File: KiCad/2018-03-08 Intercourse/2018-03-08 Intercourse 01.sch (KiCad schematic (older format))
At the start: 48 parts

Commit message: minor fixes
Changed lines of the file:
@@
 NoConn ~ 2600 7100
 NoConn ~ 2600 7000
-NoConn ~ 4800 6600
+NoConn ~ 4750 6600
 Text Notes 6300 5300 0    60   Italic 0
 Inter-Card\nConnector
@@
 L VDD #PWR?
 U 1 1 5AB0F171
-P 6100 4800
-F 0 "#PWR?" H 6100 4650 50  0001 C CNN
-F 1 "VDD" H 6100 4950 50  0000 C CNN
-F 2 "" H 6100 4800 50  0001 C CNN
-F 3 "" H 6100 4800 50  0001 C CNN
-	1    6100 4800
+P 6100 4700
+F 0 "#PWR?" H 6100 4550 50  0001 C CNN
+F 1 "VDD" H 6100 4850 50  0000 C CNN
+F 2 "" H 6100 4700 50  0001 C CNN
+F 3 "" H 6100 4700 50  0001 C CNN
+	1    6100 4700
 	1    0    0    -1
 $EndComp
@@
 	4750 6700 5400 6700
 Wire Wire Line
-	4750 6600 4800 6600
-Wire Wire Line
 	3800 5200 3900 5200

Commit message: finailzed schematic with annotations
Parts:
- removed R?: 100K, symbol R_Small
- C?: value 1μF -> 10μF
- R?: value 2K2 -> 17K
- R?: value 3K3 -> 33K
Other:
- note added: "0603\n"
- note added: "0805"
- note added: "0805\n"
- note added: ">15mil"
- note added: "?"
- note added: "X5R/X7R\n0805\n"
- note added: "±1%"
- note added: "±10PPM"
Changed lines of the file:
@@
 U 1 1 5AAA95FB
 P 3100 2100
-F 0 "C?" H 2950 2200 50  0000 L CNN
+F 0 "C?" H 2900 2100 50  0000 L CNN
 F 1 "1μF" H 2900 2000 50  0000 L CNN
 F 2 "" H 3100 2100 50  0001 C CNN
@@
 	1    3100 2100
 	1    0    0    -1
-$EndComp
-$Comp
-L R_Small R?
-U 1 1 5AAAA249
-P 2800 2600
-F 0 "R?" H 2900 2650 50  0000 L CNN
-F 1 "100K" H 2850 2550 50  0000 L CNN
-F 2 "" H 2800 2600 50  0001 C CNN
-F 3 "" H 2800 2600 50  0001 C CNN
-	1    2800 2600
-	-1   0    0    1
 $EndComp
 $Comp
@@
 U 1 1 5AAD1277
 P 4000 5200
-F 0 "Y?" V 3900 5000 50  0000 L CNN
-F 1 "26 MHz" V 4100 4800 50  0000 L CNN
+F 0 "Y?" V 4100 4700 50  0000 L CNN
+F 1 "26 MHz" V 4100 4850 50  0000 L CNN
 F 2 "" H 4000 5200 50  0001 C CNN
 F 3 "" H 4000 5200 50  0001 C CNN
@@
 P 2400 6300
 F 0 "C?" H 2200 6300 50  0000 L CNN
-F 1 "1μF" H 2150 6200 50  0000 L CNN
+F 1 "1μF" H 2200 6200 50  0000 L CNN
 F 2 "" H 2400 6300 50  0001 C CNN
 F 3 "" H 2400 6300 50  0001 C CNN
@@
 $EndComp
 $Comp
-L GND #PWR?
-U 1 1 5AB13EAF
-P 2800 2800
-F 0 "#PWR?" H 2800 2550 50  0001 C CNN
-F 1 "GND" H 2800 2650 50  0000 C CNN
-F 2 "" H 2800 2800 50  0001 C CNN
-F 3 "" H 2800 2800 50  0001 C CNN
-	1    2800 2800
-	1    0    0    -1
-$EndComp
-$Comp
 L VBUS #PWR?
 U 1 1 5AB1587E
@@
 P 5900 5400
 F 0 "C?" V 5950 5450 50  0000 L CNN
-F 1 "1μF" V 6050 5350 50  0000 L CNN
+F 1 "10μF" V 6050 5300 50  0000 L CNN
 F 2 "" H 5900 5400 50  0001 C CNN
 F 3 "" H 5900 5400 50  0001 C CNN
@@
 	3200 2200 3100 2200
 Wire Wire Line
-	2800 2700 2800 2800
-Wire Wire Line
 	4200 2400 4600 2400
 Wire Wire Line
@@
 P 5850 3700
 F 0 "R?" V 5750 3850 50  0000 C CNN
-F 1 "2K2" V 5750 3650 50  0000 C CNN
+F 1 "17K" V 5750 3650 50  0000 C CNN
 F 2 "" V 5780 3700 50  0001 C CNN
 F 3 "" H 5850 3700 50  0001 C CNN
@@
 P 5850 4100
 F 0 "R?" V 5950 4250 50  0000 C CNN
-F 1 "3K3" V 5950 4050 50  0000 C CNN
+F 1 "33K" V 5950 4050 50  0000 C CNN
 F 2 "" V 5780 4100 50  0001 C CNN
 F 3 "" H 5850 4100 50  0001 C CNN
@@
 	6100 3900 6200 3900
 Connection ~ 6200 3900
-Text Notes 6300 4050 0    60   Italic 0
+Text Notes 6300 4000 0    60   Italic 0
 Check if\nconnected\nto USB
 Text GLabel 3100 2600 3    60   Input ~ 0
@@
 Connection ~ 1500 4900
 Wire Wire Line
-	2800 2400 2800 2500
-Connection ~ 2800 2400
-Wire Wire Line
 	3200 2500 3100 2500
 Wire Wire Line
@@
 Wire Wire Line
 	2400 5700 2400 6200
+Text Notes 1200 7050 0    30   ~ 0
+0805
+Text Notes 3900 5450 1    30   ~ 0
+±10PPM
+Text Notes 3600 5100 3    30   ~ 0
+±1%
+Text Notes 1300 6400 0    30   ~ 0
+>15mil
+Text Notes 2300 5500 0    30   ~ 0
+>15mil
+Text Notes 4600 8300 0    30   ~ 0
+>15mil
+Text Notes 2200 6250 0    30   ~ 0
+0805
+Text Notes 1800 6450 0    30   ~ 0
+0603\n
+Text Notes 1600 7050 0    30   ~ 0
+0603\n
+Text Notes 3850 4950 0    30   ~ 0
+0603\n
+Text Notes 4050 4950 0    30   ~ 0
+0603\n
+Text Notes 5900 5150 1    30   ~ 0
+0805\n
+Text Notes 5500 7600 0    30   ~ 0
+0805
+Text Notes 4200 9250 0    30   ~ 0
+0805
+Text Notes 2900 8550 0    30   ~ 0
+0805
+Text Notes 2900 8900 0    30   ~ 0
+0805
+Text Notes 6300 4100 0    30   ~ 0
+0805\n
+Text Notes 4750 2700 2    30   ~ 0
+0805\n
+Text Notes 2900 2050 0    30   ~ 0
+X5R/X7R\n0805\n
+Text Notes 3600 3800 0    30   ~ 0
+0805\n
+Text Notes 5800 5000 0    120  ~ 24
+?
+Text Notes 5400 1500 0    30   ~ 0
+0805\n
 $EndSCHEMATC

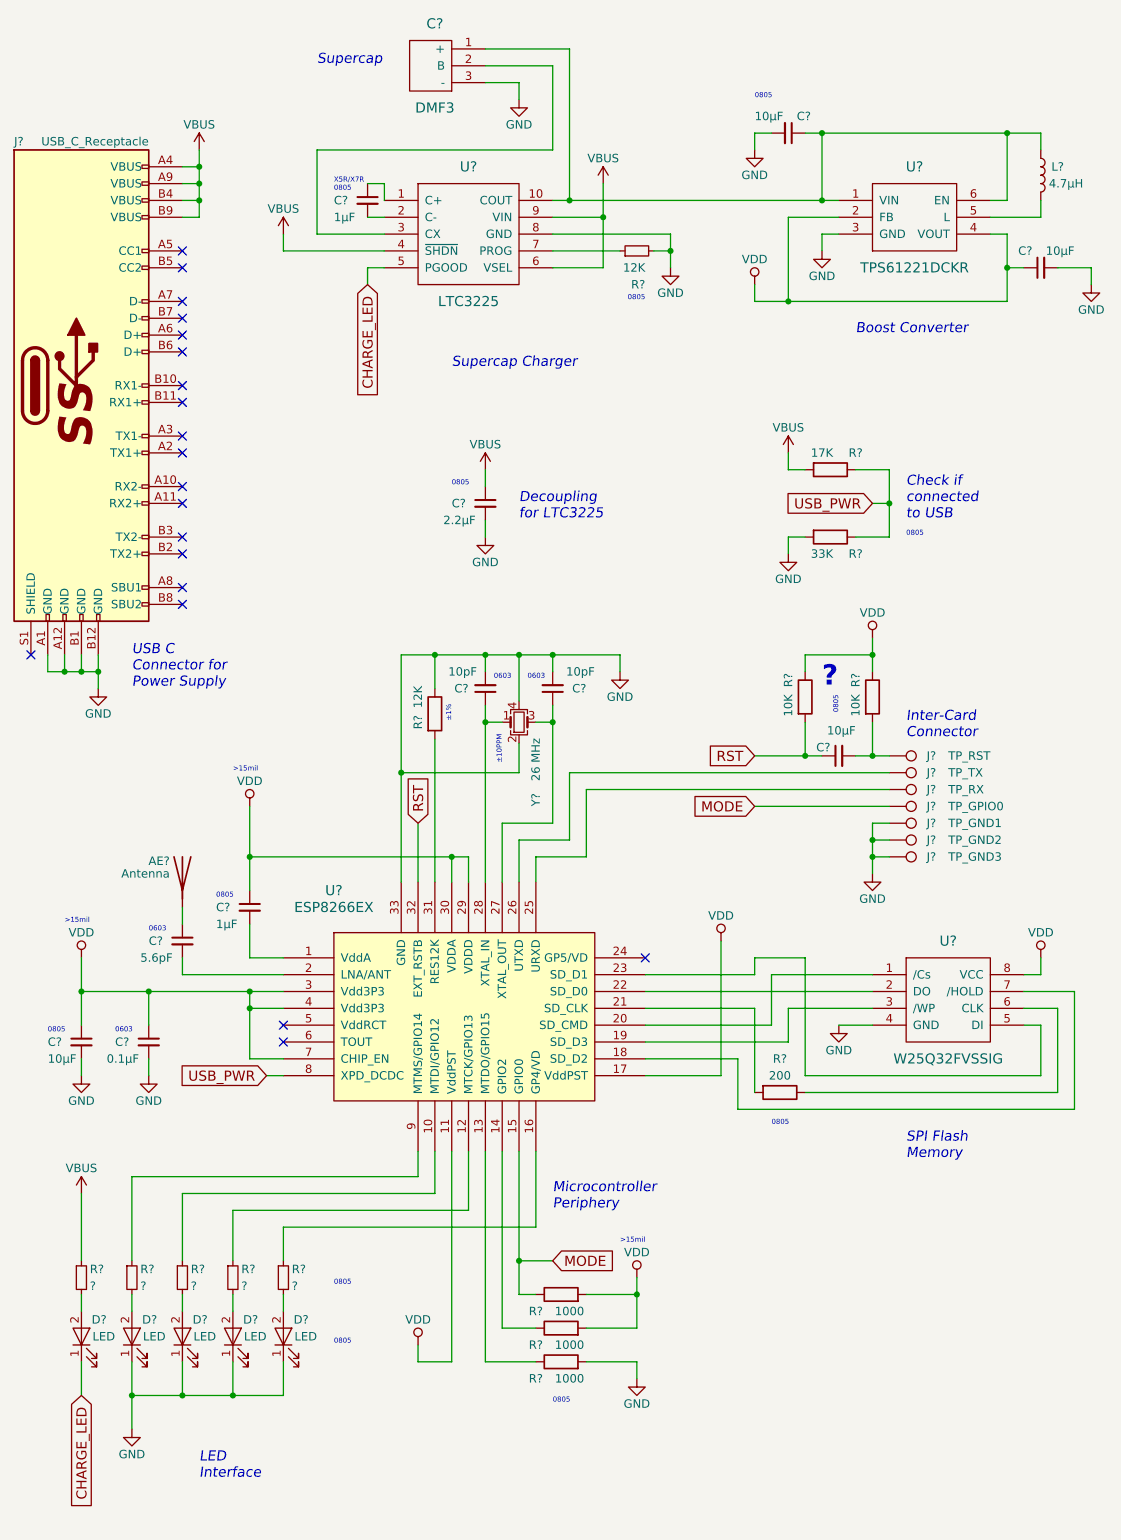
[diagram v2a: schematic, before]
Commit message: updated library paths
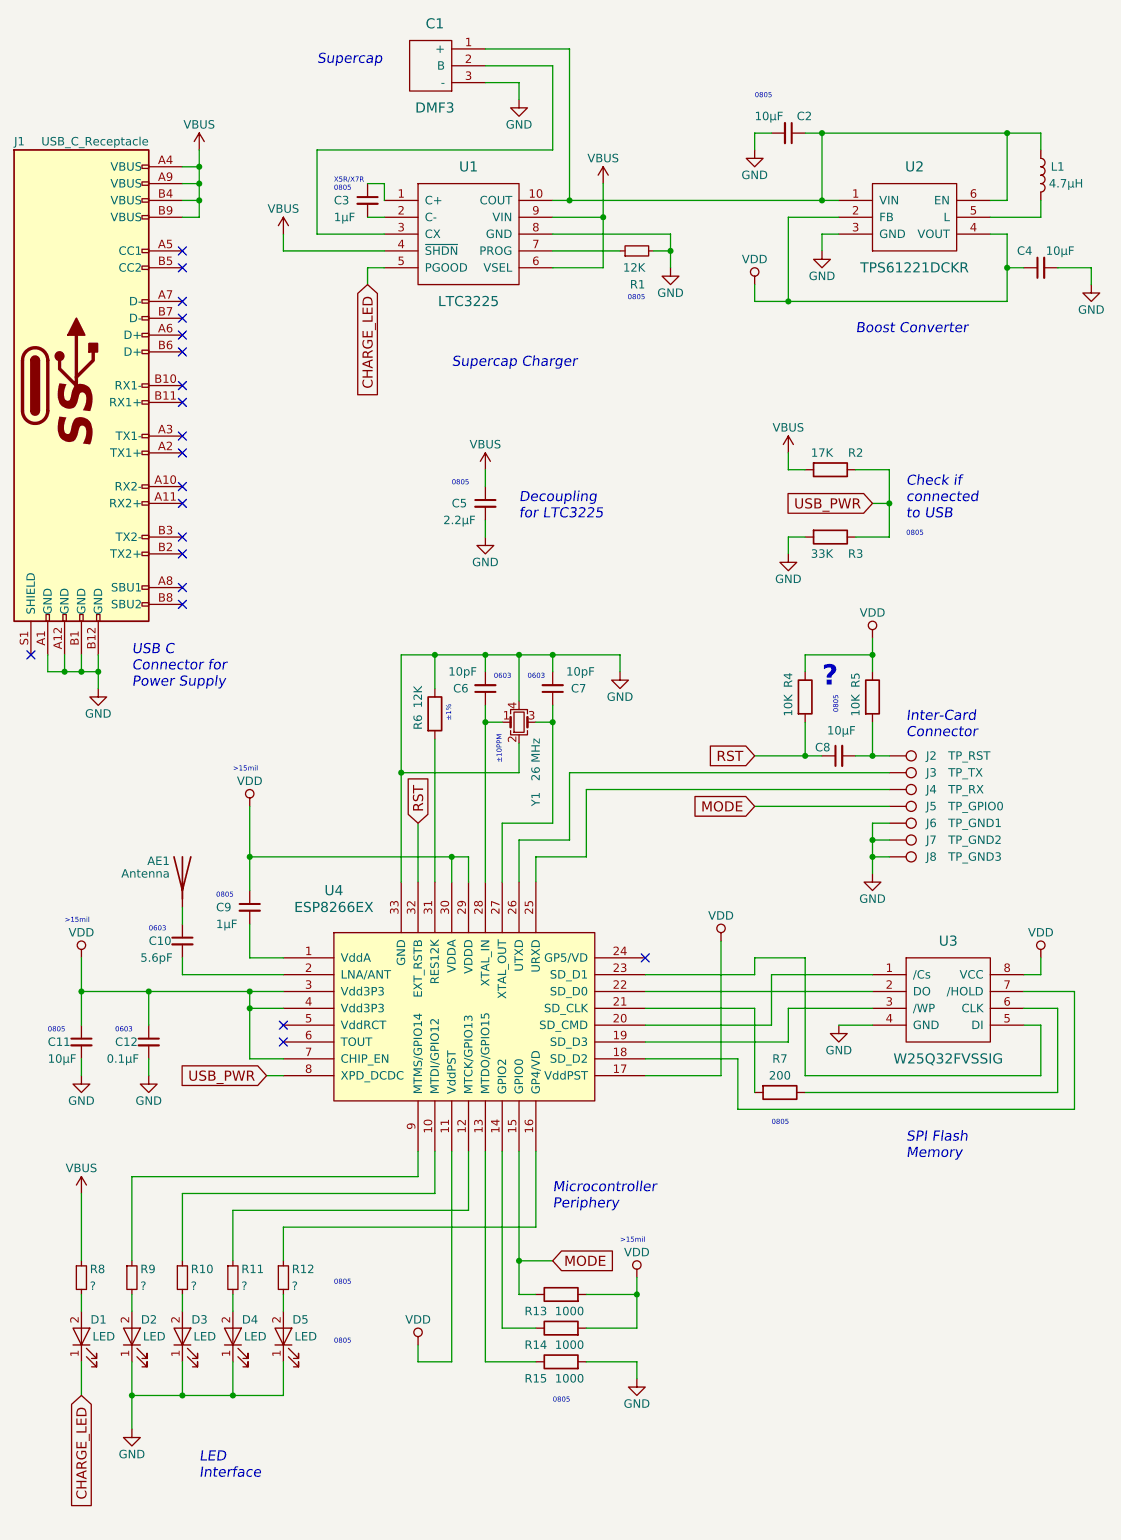
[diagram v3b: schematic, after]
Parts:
- gave numbers to parts that had none: 47

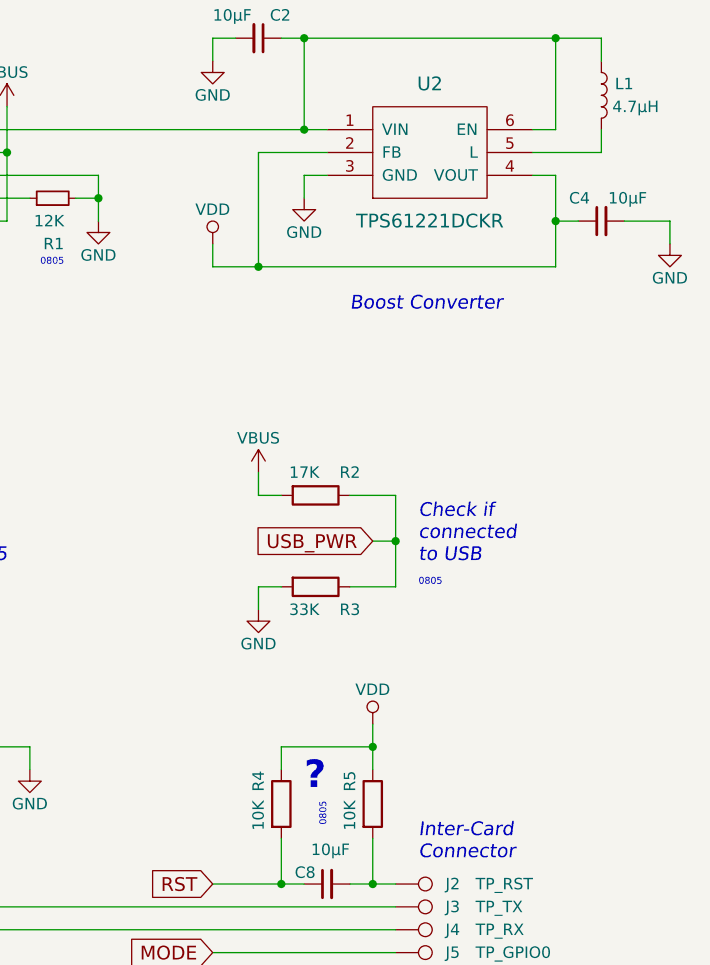
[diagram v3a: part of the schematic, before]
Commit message: created additional footprints and completed footprint reference
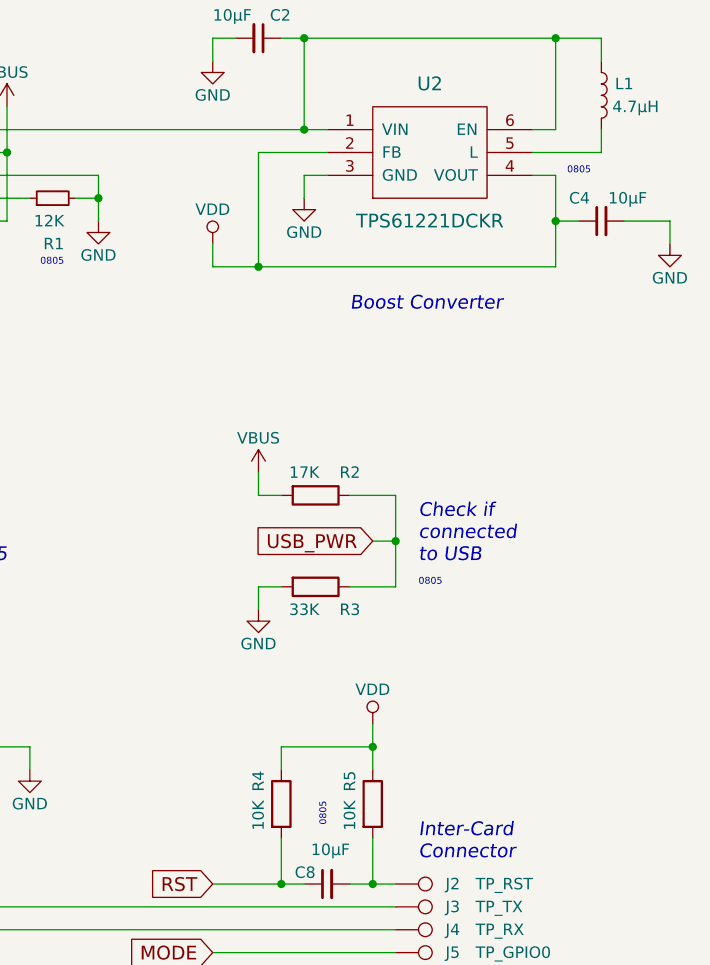
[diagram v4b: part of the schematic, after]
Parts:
- AE1: footprint (none) -> MyAntennas:AN91445
- C1: footprint (none) -> Murata_DMF3Z:Murata_DMF3Z
- C10, C12, C6, C7, C9: footprint (none) -> Capacitors_SMD:C_0603_HandSoldering
- C11, C2, C3, C4, C5, C8: footprint (none) -> Capacitors_SMD:C_0805_HandSoldering
- D1, D2, D3, D4, D5: footprint (none) -> LEDs:LED_0805_HandSoldering
- J1: footprint (none) -> Connectors_USB:USB_C_Receptacle_Amphenol_12401610E4-2A
- J2, J3, J4, J5, J6, J7, J8: footprint (none) -> C_Connectors:C_Connector_2mm
- L1: footprint (none) -> C_Connectors:LQH3NPN4R7MJRL
- R1, R10, R11, R12, R13, R14, R15, R2, R3, R4, R5, R6, R7, R8, R9: footprint (none) -> Resistors_SMD:R_0805_HandSoldering
- U1: footprint (none) -> Housings_DFN_QFN:DFN-10-1EP_2x3mm_Pitch0.5mm
- U2: footprint (none) -> TO_SOT_Packages_SMD:SC-70-8_Handsoldering
- U3: footprint (none) -> Housings_SOIC:SOIC-8_3.9x4.9mm_Pitch1.27mm
- U4: footprint (none) -> Housings_DFN_QFN:QFN-32-1EP_5x5mm_Pitch0.5mm
- Y1: footprint (none) -> Crystals:Crystal_SMD_Abracon_ABM8G-4pin_3.2x2.5mm
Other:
- note removed: "?"

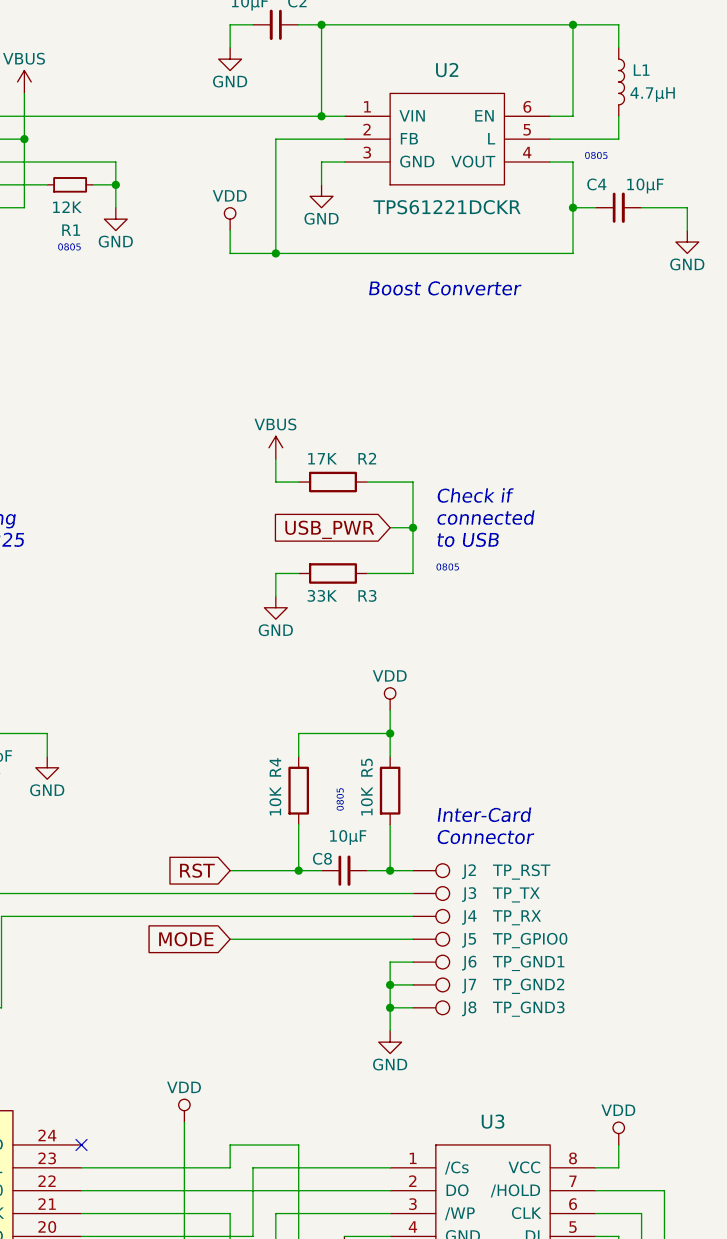
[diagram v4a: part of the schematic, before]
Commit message: created netlist and created pcb
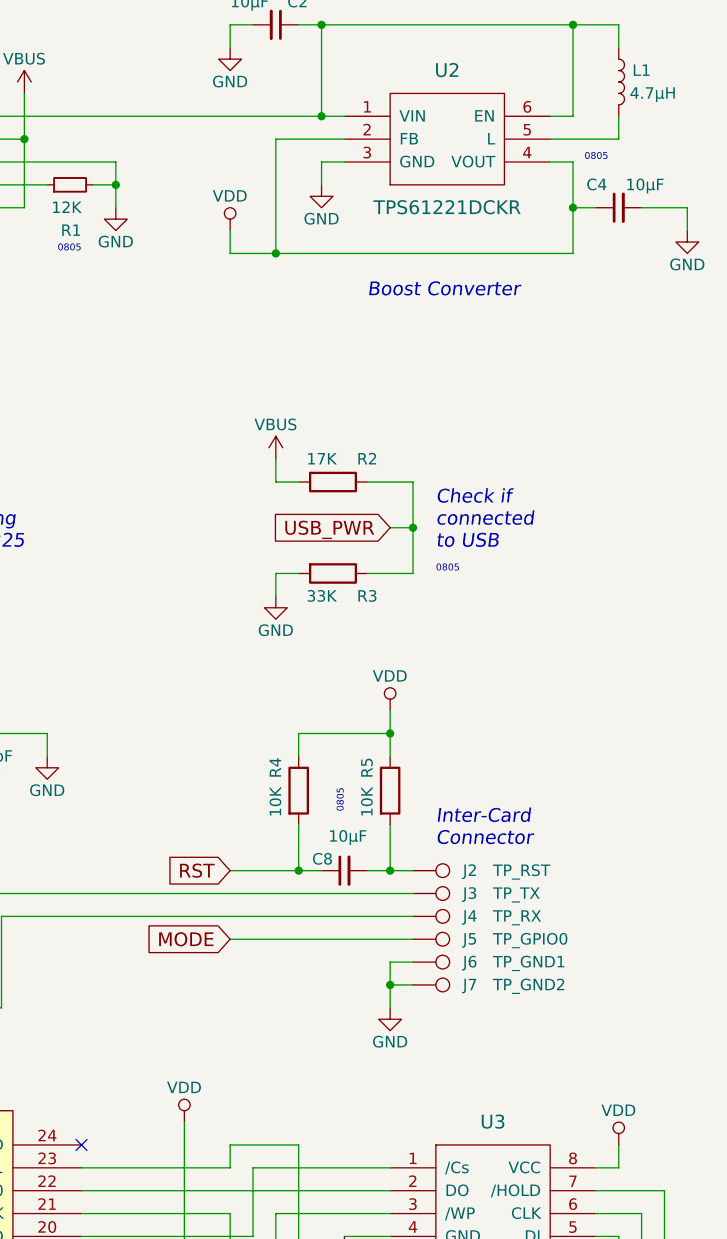
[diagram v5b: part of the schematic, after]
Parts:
- removed J8: TP_GND3, C_Connectors:C_Connector_2mm, symbol TEST_1P
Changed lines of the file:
@@
 L GND #PWR05
 U 1 1 5AB0526A
-P 6100 6100
-F 0 "#PWR05" H 6100 5850 50  0001 C CNN
-F 1 "GND" H 6100 5950 50  0000 C CNN
-F 2 "" H 6100 6100 50  0001 C CNN
-F 3 "" H 6100 6100 50  0001 C CNN
-	1    6100 6100
+P 6100 6000
+F 0 "#PWR05" H 6100 5750 50  0001 C CNN
+F 1 "GND" H 6100 5850 50  0000 C CNN
+F 2 "" H 6100 6000 50  0001 C CNN
+F 3 "" H 6100 6000 50  0001 C CNN
+	1    6100 6000
 	1    0    0    -1
 $EndComp
@@
 	0    1    1    0
 $EndComp
-$Comp
-L TEST_1P J8
-U 1 1 5AB30E56
-P 6200 6000
-F 0 "J8" V 6200 6250 50  0000 C CNN
-F 1 "TP_GND3" V 6200 6350 50  0000 L CNN
-F 2 "C_Connectors:C_Connector_2mm" H 6400 6000 50  0001 C CNN
-F 3 "" H 6400 6000 50  0001 C CNN
-	1    6200 6000
-	0    1    1    0
-$EndComp
 Wire Wire Line
 	4200 2300 4900 2300
@@
 	6800 2300 6900 2300
 Wire Wire Line
-	6900 2300 6900 2700
-Wire Wire Line
-	6900 2700 5400 2700
+	6900 2700 6900 2300
+Wire Wire Line
+	5400 2700 6900 2700
 Wire Wire Line
 	5600 2700 5600 2200
@@
 	6200 5800 6100 5800
 Wire Wire Line
-	6100 5800 6100 6100
+	6100 5800 6100 6000
 Wire Wire Line
 	6200 5900 6100 5900
 Connection ~ 6100 5900
 Wire Wire Line
-	6200 6000 6100 6000
-Connection ~ 6100 6000
-Wire Wire Line
 	2000 8000 3500 8000

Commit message: backup of layouting process
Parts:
- U2: footprint TO_SOT_Packages_SMD:SC-70-8_Handsoldering -> sc_70-6:sc_70-6
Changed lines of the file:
@@
 F 0 "U2" H 6350 2500 60  0000 C CNN
 F 1 "TPS61221DCKR" H 6350 1900 60  0000 C CNN
-F 2 "TO_SOT_Packages_SMD:SC-70-8_Handsoldering" H 6350 2200 60  0001 C CNN
+F 2 "sc_70-6:sc_70-6" H 6350 2200 60  0001 C CNN
 F 3 "" H 6350 2200 60  0001 C CNN
 	1    6350 2200
@@
 	6800 2300 6900 2300
 Wire Wire Line
-	6900 2700 6900 2300
-Wire Wire Line
-	5400 2700 6900 2700
+	6900 2300 6900 2700
+Wire Wire Line
+	6900 2700 5400 2700
 Wire Wire Line
 	5600 2700 5600 2200

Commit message: ready to route
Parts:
- added J8: TP_GND3, C_Connectors:C_Connector_2mm, symbol TEST_1P
- J5: footprint C_Connectors:C_Connector_2mm -> Measurement_Points:Measurement_Point_Round-SMD-Pad_Small
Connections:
- net GND: now also J8.1
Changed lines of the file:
@@
 L GND #PWR05
 U 1 1 5AB0526A
-P 6100 6000
-F 0 "#PWR05" H 6100 5750 50  0001 C CNN
-F 1 "GND" H 6100 5850 50  0000 C CNN
-F 2 "" H 6100 6000 50  0001 C CNN
-F 3 "" H 6100 6000 50  0001 C CNN
-	1    6100 6000
+P 6100 6100
+F 0 "#PWR05" H 6100 5850 50  0001 C CNN
+F 1 "GND" H 6100 5950 50  0000 C CNN
+F 2 "" H 6100 6100 50  0001 C CNN
+F 3 "" H 6100 6100 50  0001 C CNN
+	1    6100 6100
 	1    0    0    -1
 $EndComp
@@
 F 0 "J5" V 6200 5950 50  0000 C CNN
 F 1 "TP_GPIO0" V 6200 6050 50  0000 L CNN
-F 2 "C_Connectors:C_Connector_2mm" H 6400 5700 50  0001 C CNN
+F 2 "Measurement_Points:Measurement_Point_Round-SMD-Pad_Small" H 6400 5700 50  0001 C CNN
 F 3 "" H 6400 5700 50  0001 C CNN
 	1    6200 5700
@@
 	6200 5800 6100 5800
 Wire Wire Line
-	6100 5800 6100 6000
+	6100 5800 6100 6100
 Wire Wire Line
 	6200 5900 6100 5900
@@
 Text Notes 6950 2300 0    30   ~ 0
 0805\n
+$Comp
+L TEST_1P J8
+U 1 1 5AB7C6F7
+P 6200 6000
+F 0 "J8" V 6200 6250 50  0000 C CNN
+F 1 "TP_GND3" V 6200 6350 50  0000 L CNN
+F 2 "C_Connectors:C_Connector_2mm" H 6400 6000 50  0001 C CNN
+F 3 "" H 6400 6000 50  0001 C CNN
+	1    6200 6000
+	0    1    1    0
+$EndComp
+Wire Wire Line
+	6200 6000 6100 6000
+Connection ~ 6100 6000
 $EndSCHEMATC
